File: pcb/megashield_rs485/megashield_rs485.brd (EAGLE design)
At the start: 101.6 x 53.3 mm, 16 parts

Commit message: PCB template
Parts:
- removed JP10: (no value), SparkFun:1X06_LOCK
- removed JP11, JP12: (no value), SparkFun:1X02_LOCK
- removed JP3, JP4, JP5, JP6, JP7: (no value), SparkFun:1X08_LOCK
- removed JP8, JP9: M16LOCK, SparkFun:1X16_LOCK
- removed LED1: Red, SparkFun:LED5MM
- removed LED2: Green, SparkFun:LED5MM
- removed R1, R2: 330, SparkFun:AXIAL-0.3
- removed R3: 10k, SparkFun:AXIAL-0.3
- removed S1: (no value), SparkFun:TACTILE-PTH
- added J1, J2, J3, J8, J9: (no value), mecatronica_eagle_lib:1X08_LONGPADS
- added J10: (no value), mecatronica_eagle_lib:1X06_LONGPADS
- added J4, J5: (no value), mecatronica_eagle_lib:1X16
- added J6, J7: (no value), mecatronica_eagle_lib:1X02
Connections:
- removed net GND: JP10.4, JP10.5, JP11.1, JP11.2, JP3.7, LED1.K, LED2.K, S1.1, S1.2
- removed net N$126: LED1.A, R1.P$1
- removed net N$127: LED2.A, R2.P$1
- new net ASD: J1.7, J10.4, J10.5, J7.1, J7.2
- net 3.3: now also J10.2; no longer JP10.2
- net 5V: now also J10.3; no longer JP10.3, R1.P$2, R3.P$2
- net 5V@1: now also J6.1, J6.2; no longer JP12.1, JP12.2
- net A0: now also J9.1; no longer JP7.1
- net A1: now also J9.2; no longer JP7.2
- net A10: now also J8.3; no longer JP6.3
- net A11: now also J8.4; no longer JP6.4
- net A12: now also J8.5; no longer JP6.5
- net A13: now also J8.6; no longer JP6.6
- net A14: now also J8.7; no longer JP6.7
- net A15: now also J8.8; no longer JP6.8
- net A2: now also J9.3; no longer JP7.3
- net A3: now also J9.4; no longer JP7.4
- net A4: now also J9.5; no longer JP7.5
- net A5: now also J9.6; no longer JP7.6
- net A6: now also J9.7; no longer JP7.7
- net A7: now also J9.8; no longer JP7.8
- net A8: now also J8.1; no longer JP6.1
- net A9: now also J8.2; no longer JP6.2
- net AREF: now also J1.8; no longer JP3.8
- net D10: now also J1.3; no longer JP3.3
- net D11: now also J1.4; no longer JP3.4
- net D12: now also J1.5; no longer JP3.5
- net D13: now also J1.6; no longer JP3.6, R2.P$2
- net D14: now also J3.8; no longer JP5.8
- net D15: now also J3.7; no longer JP5.7
- net D16: now also J3.6; no longer JP5.6
- net D17: now also J3.5; no longer JP5.5
- net D18: now also J3.4; no longer JP5.4
- net D19: now also J3.3; no longer JP5.3
- net D2: now also J2.3; no longer JP4.3
- net D22: now also J5.1; no longer JP9.1
- net D23: now also J4.16; no longer JP8.16
- net D24: now also J5.2; no longer JP9.2
- net D25: now also J4.15; no longer JP8.15
- net D26: now also J5.3; no longer JP9.3
- net D27: now also J4.14; no longer JP8.14
- net D28: now also J5.4; no longer JP9.4
- net D29: now also J4.13; no longer JP8.13
- net D3: now also J2.4; no longer JP4.4
- net D30: now also J5.5; no longer JP9.5
- net D31: now also J4.12; no longer JP8.12
- net D32: now also J5.6; no longer JP9.6
- net D33: now also J4.11; no longer JP8.11
- net D34: now also J5.7; no longer JP9.7
- net D35: now also J4.10; no longer JP8.10
- net D36: now also J5.8; no longer JP9.8
- net D37: now also J4.9; no longer JP8.9
- net D38: now also J5.9; no longer JP9.9
- net D39: now also J4.8; no longer JP8.8
- net D4: now also J2.5; no longer JP4.5
- net D40: now also J5.10; no longer JP9.10
- net D41: now also J4.7; no longer JP8.7
- net D42: now also J5.11; no longer JP9.11
- net D43: now also J4.6; no longer JP8.6
- net D44: now also J5.12; no longer JP9.12
- net D45: now also J4.5; no longer JP8.5
- net D46: now also J5.13; no longer JP9.13
- net D47: now also J4.4; no longer JP8.4
- net D48: now also J5.14; no longer JP9.14
- net D49: now also J4.3; no longer JP8.3
- net D5: now also J2.6; no longer JP4.6
- net D50: now also J5.15; no longer JP9.15
- net D51: now also J4.2; no longer JP8.2
- net D52: now also J5.16; no longer JP9.16
- net D53: now also J4.1; no longer JP8.1
- net D6: now also J2.7; no longer JP4.7
- net D7: now also J2.8; no longer JP4.8
- net D8: now also J1.1; no longer JP3.1
- net D9: now also J1.2; no longer JP3.2
- net RES: now also J10.1; no longer JP10.1, R3.P$1, S1.3, S1.4
- net RX0: now also J2.1; no longer JP4.1
- net SCL: now also J3.1; no longer JP5.1
- net SDA: now also J3.2; no longer JP5.2
- net TX1: now also J2.2; no longer JP4.2
- net VIN: now also J10.6; no longer JP10.6
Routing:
- net 5V@1: track 99.8 -> 0.00 mm, vias 30 -> 0
- net D13: track 43.4 -> 0.00 mm
- net 5V: track 26.0 -> 0.00 mm
- net RES: track 18.6 -> 0.00 mm
- net N$127: track 14.8 -> 0.00 mm
- net N$126: track 4.91 -> 0.00 mm
- net VIN: track 0.51 -> 0.00 mm
- net 3.3: track 0.51 -> 0.00 mm
- added copper zone on layer 1, net ASD
- added copper zone on layer 16, net ASD
- removed copper zone on layer 1, net GND
- removed copper zone on layer 16, net GND
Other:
- board text removed: "5V Bus"
- board text removed: "GND Bus"
- board text removed: "POWER"
- board text removed: "RESET"
- board text removed: "STAT"

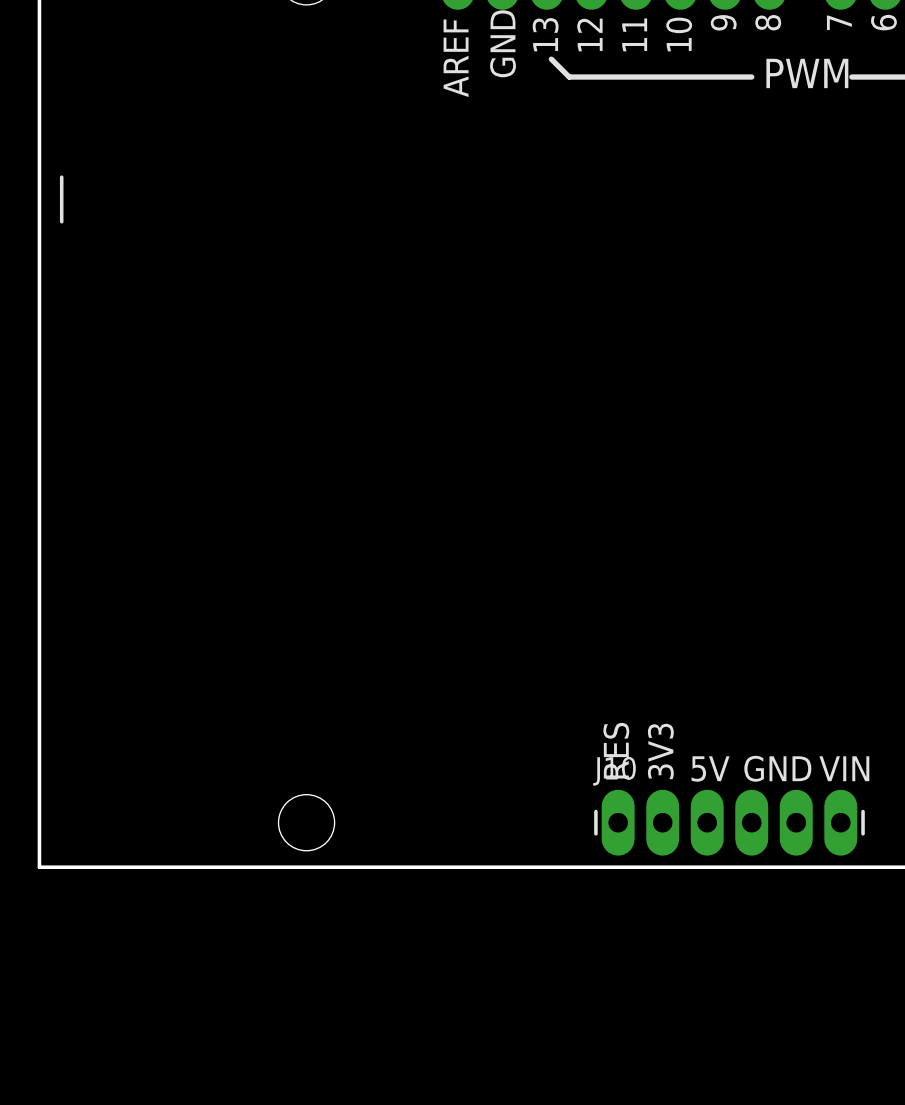
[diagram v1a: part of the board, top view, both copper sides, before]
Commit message: Add rs485 transceiver
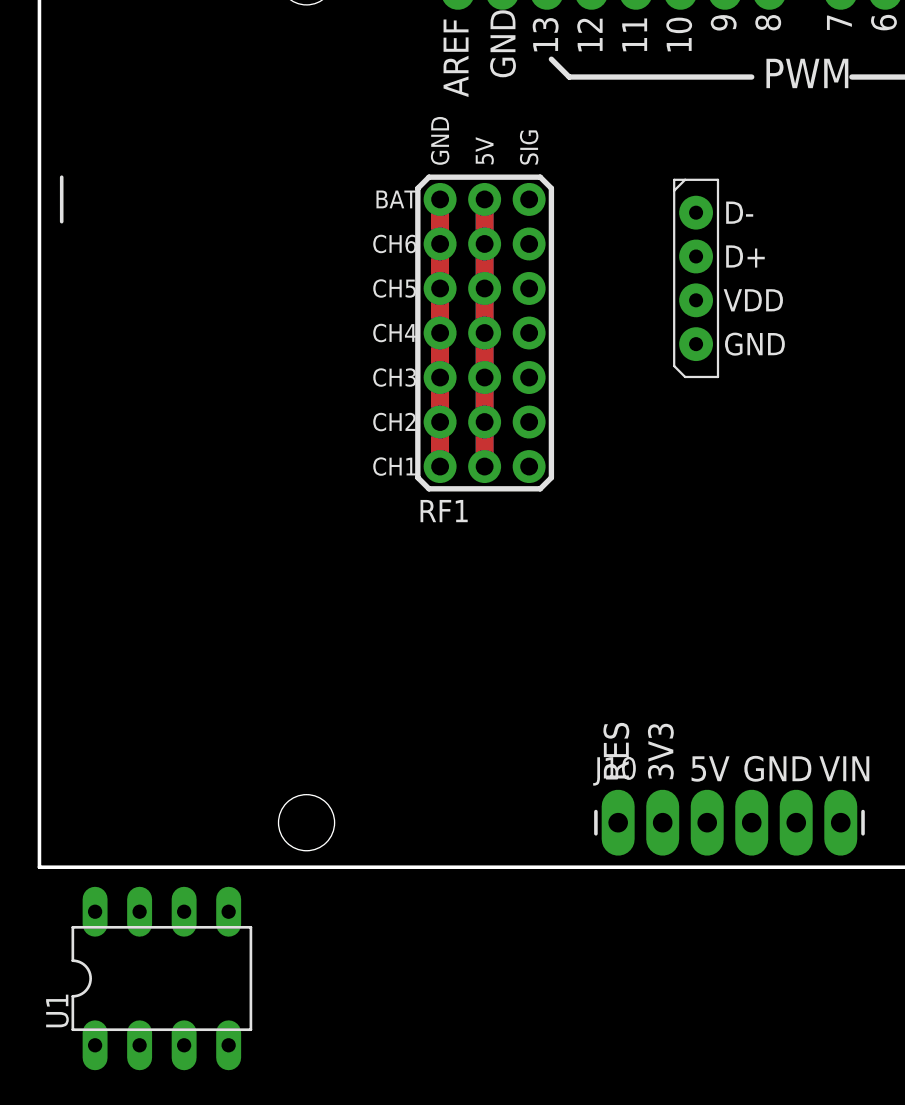
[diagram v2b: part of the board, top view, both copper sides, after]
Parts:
- added J11: DYNAMIXEL_RS485, mecatronica_eagle_lib:DYNAMIXEL_SPOX_04
- added RF1: FS_R6B, mecatronica_eagle_lib:FS_R6B
- added U1: SN75176B, mecatronica_eagle_lib:DIL08
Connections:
- removed net 5V@1: J6.1, J6.2
- removed net ASD: J1.7, J10.4, J10.5, J7.1, J7.2
- new net GND: J1.7, J10.4, J10.5, J11.1, J7.1, J7.2, RF1.GND@1, RF1.GND@2, RF1.GND@3, RF1.GND@4, RF1.GND@5, RF1.GND@6, RF1.GND@7
- new net N$3: RF1.CH1
- new net N$4: RF1.CH2
- new net N$5: RF1.CH3
- new net N$6: RF1.CH4
- new net N$7: RF1.CH5
- new net N$8: RF1.CH6
- new net VDD: J11.2
- net 5V: now also J6.1, J6.2, RF1.VCC@1, RF1.VCC@2, RF1.VCC@3, RF1.VCC@4, RF1.VCC@5, RF1.VCC@6, RF1.VCC@7
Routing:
- added copper zone on layer 1, net GND
- added copper zone on layer 16, net GND
- removed copper zone on layer 1, net ASD
- removed copper zone on layer 16, net ASD

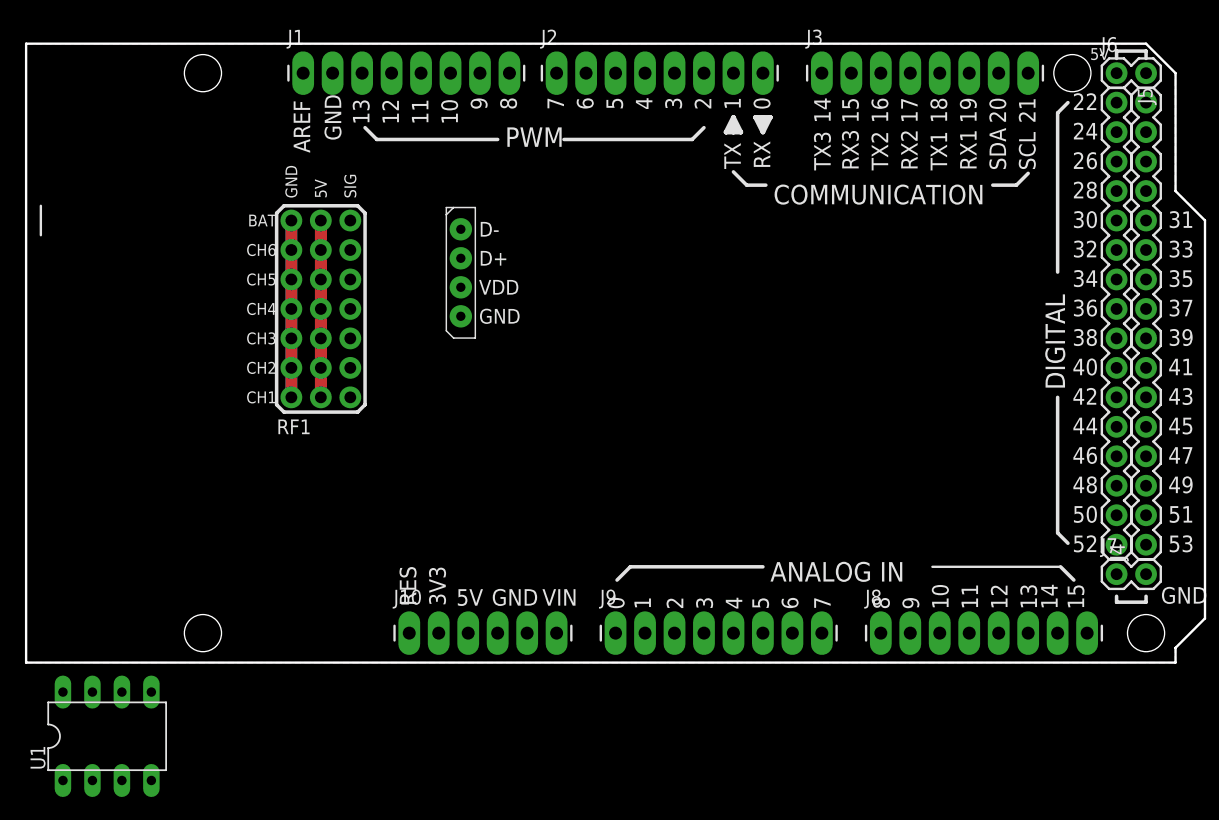
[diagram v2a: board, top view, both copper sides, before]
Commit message: Add analog inputs
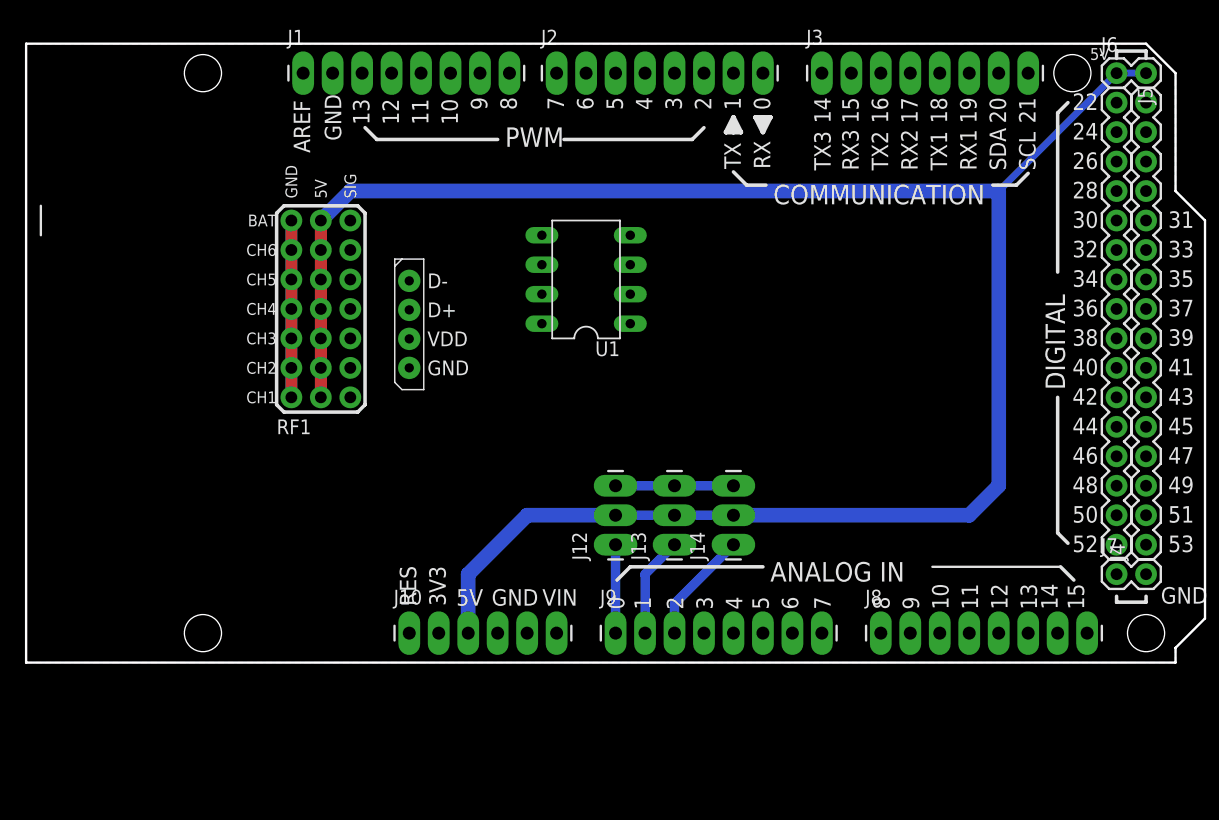
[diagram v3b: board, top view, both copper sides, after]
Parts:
- added J12, J13, J14: (no value), mecatronica_eagle_lib:1X03_LONGPADS
- moved U1 57.0 mm to (48.3, 33.0), turned to 90 degrees
- moved J11 6.29 mm to (33.0, 25.4)
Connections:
- net 5V: now also J12.2, J13.2, J14.2
- net A0: now also J12.1
- net A1: now also J13.1
- net A2: now also J14.1
- net GND: now also J12.3, J13.3, J14.3
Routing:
- net 5V: track 0.00 -> 155.7 mm
- net GND: track 0.00 -> 10.2 mm
- net A2: track 0.00 -> 9.72 mm
- net A1: track 0.00 -> 8.67 mm
- net A0: track 0.00 -> 7.62 mm
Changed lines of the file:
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@@
 <setting verticaltext="up"/>
 </settings>
-<grid distance="25" unitdist="mil" unit="mil" style="lines" multiple="1" display="yes" altdistance="50" altunitdist="mil" altunit="mil"/>
+<grid distance="100" unitdist="mil" unit="mil" style="lines" multiple="1" display="yes" altdistance="50" altunitdist="mil" altunit="mil"/>
 <layers>
 <layer number="1" name="Top" color="4" fill="1" visible="yes" active="yes"/>
@@
 <element name="J10" library="mecatronica_eagle_lib" package="1X06_LONGPADS" value="" x="33.02" y="2.54"/>
 <element name="RF1" library="mecatronica_eagle_lib" package="FS_R6B" value="FS_R6B" x="22.86" y="38.1"/>
-<element name="J11" library="mecatronica_eagle_lib" package="DYNAMIXEL_SPOX_04" value="DYNAMIXEL_RS485" x="37.465" y="29.845" rot="R90"/>
-<element name="U1" library="mecatronica_eagle_lib" package="DIL08" value="SN75176B" x="6.985" y="-6.35"/>
+<element name="J11" library="mecatronica_eagle_lib" package="DYNAMIXEL_SPOX_04" value="DYNAMIXEL_RS485" x="33.02" y="25.4" rot="R90"/>
+<element name="U1" library="mecatronica_eagle_lib" package="DIL08" value="SN75176B" x="48.26" y="33.02" rot="R90"/>
+<element name="J12" library="mecatronica_eagle_lib" package="1X03_LONGPADS" value="" x="50.8" y="10.16" rot="R90"/>
+<element name="J13" library="mecatronica_eagle_lib" package="1X03_LONGPADS" value="" x="55.88" y="10.16" rot="R90"/>
+<element name="J14" library="mecatronica_eagle_lib" package="1X03_LONGPADS" value="" x="60.96" y="10.16" rot="R90"/>
 </elements>
 <signals>
@@
 <contactref element="J6" pad="2"/>
 <contactref element="J6" pad="1"/>
-<wire x1="93.98" y1="50.8" x2="96.52" y2="50.8" width="0" layer="19" extent="1-1"/>
-<wire x1="38.1" y1="2.54" x2="93.98" y2="50.8" width="0" layer="19" extent="1-1"/>
-<wire x1="25.4" y1="22.86" x2="38.1" y2="2.54" width="0" layer="19" extent="1-1"/>
-<wire x1="25.4" y1="35.56" x2="25.4" y2="38.1" width="0" layer="19" extent="1-1"/>
+<contactref element="J12" pad="2"/>
+<contactref element="J13" pad="2"/>
+<contactref element="J14" pad="2"/>
+<wire x1="60.96" y1="12.7" x2="55.88" y2="12.7" width="0.8128" layer="16"/>
+<wire x1="50.8" y1="12.7" x2="55.88" y2="12.7" width="0.8128" layer="16"/>
+<wire x1="38.1" y1="2.54" x2="38.1" y2="7.62" width="1.27" layer="16"/>
+<wire x1="38.1" y1="7.62" x2="43.18" y2="12.7" width="1.27" layer="16"/>
+<wire x1="43.18" y1="12.7" x2="50.8" y2="12.7" width="1.27" layer="16"/>
+<wire x1="96.52" y1="50.8" x2="93.98" y2="50.8" width="0.6096" layer="16"/>
+<wire x1="93.98" y1="50.8" x2="83.82" y2="40.64" width="0.6096" layer="16"/>
+<wire x1="83.82" y1="40.64" x2="27.94" y2="40.64" width="1.27" layer="16"/>
+<wire x1="60.96" y1="12.7" x2="81.28" y2="12.7" width="1.27" layer="16"/>
+<wire x1="81.28" y1="12.7" x2="83.82" y2="15.24" width="1.27" layer="16"/>
+<wire x1="83.82" y1="15.24" x2="83.82" y2="40.64" width="1.27" layer="16"/>
+<wire x1="27.94" y1="40.64" x2="25.4" y2="38.1" width="1.27" layer="16"/>
 <wire x1="25.4" y1="33.02" x2="25.4" y2="35.56" width="0" layer="19" extent="1-1"/>
 <wire x1="25.4" y1="30.48" x2="25.4" y2="33.02" width="0" layer="19" extent="1-1"/>
 <wire x1="25.4" y1="27.94" x2="25.4" y2="30.48" width="0" layer="19" extent="1-1"/>
-<wire x1="25.4" y1="25.4" x2="25.4" y2="22.86" width="0" layer="19" extent="1-1"/>
+<wire x1="25.4" y1="25.4" x2="25.4" y2="27.94" width="0" layer="19" extent="1-1"/>
+<wire x1="25.4" y1="38.1" x2="25.4" y2="35.56" width="0" layer="19" extent="1-1"/>
 </signal>
 <signal name="D13">
@@
 <signal name="A0">
 <contactref element="J9" pad="1"/>
+<contactref element="J12" pad="1"/>
+<wire x1="50.8" y1="2.54" x2="50.8" y2="10.16" width="0.8128" layer="16"/>
 </signal>
 <signal name="A1">
 <contactref element="J9" pad="2"/>
+<contactref element="J13" pad="1"/>
+<wire x1="53.34" y1="2.54" x2="53.34" y2="7.62" width="0.8128" layer="16"/>
+<wire x1="53.34" y1="7.62" x2="55.88" y2="10.16" width="0.8128" layer="16"/>
 </signal>
 <signal name="A2">
 <contactref element="J9" pad="3"/>
+<contactref element="J14" pad="1"/>
+<wire x1="55.88" y1="2.54" x2="55.88" y2="5.08" width="0.8128" layer="16"/>
+<wire x1="55.88" y1="5.08" x2="60.96" y2="10.16" width="0.8128" layer="16"/>
 </signal>
 <signal name="A3">
@@
 </polygon>
 <contactref element="J1" pad="7"/>
-<wire x1="93.98" y1="7.62" x2="96.52" y2="7.62" width="0" layer="19" extent="1-1"/>
-<wire x1="43.18" y1="2.54" x2="93.98" y2="7.62" width="0" layer="19" extent="1-1"/>
-<wire x1="40.64" y1="2.54" x2="43.18" y2="2.54" width="0" layer="19" extent="1-1"/>
-<wire x1="22.86" y1="22.86" x2="40.64" y2="2.54" width="0" layer="19" extent="1-1"/>
-<wire x1="22.86" y1="35.56" x2="22.86" y2="38.1" width="0" layer="19" extent="1-1"/>
-<wire x1="22.86" y1="33.02" x2="22.86" y2="35.56" width="0" layer="19" extent="1-1"/>
-<wire x1="22.86" y1="30.48" x2="22.86" y2="33.02" width="0" layer="19" extent="1-1"/>
-<wire x1="22.86" y1="27.94" x2="22.86" y2="30.48" width="0" layer="19" extent="1-1"/>
-<wire x1="22.86" y1="25.4" x2="22.86" y2="22.86" width="0" layer="19" extent="1-1"/>
-<wire x1="37.465" y1="29.845" x2="22.86" y2="30.48" width="0" layer="19" extent="1-1"/>
-<wire x1="39.116" y1="50.8" x2="22.86" y2="38.1" width="0" layer="19" extent="1-1"/>
+<contactref element="J14" pad="3"/>
+<contactref element="J12" pad="3"/>
+<contactref element="J13" pad="3"/>
+<wire x1="50.8" y1="15.24" x2="55.88" y2="15.24" width="0.8128" layer="16"/>
+<wire x1="60.96" y1="15.24" x2="55.88" y2="15.24" width="0.8128" layer="16"/>
 </signal>
 <signal name="N$3">
